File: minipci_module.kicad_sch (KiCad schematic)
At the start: 3 parts, among them Con2 2041119-1

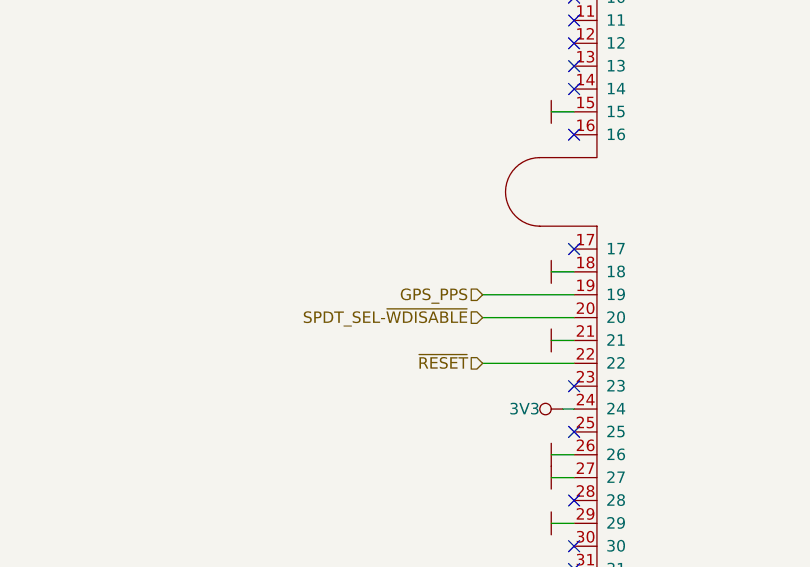
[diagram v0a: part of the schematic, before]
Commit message: Applied issue and regenerated gerbers
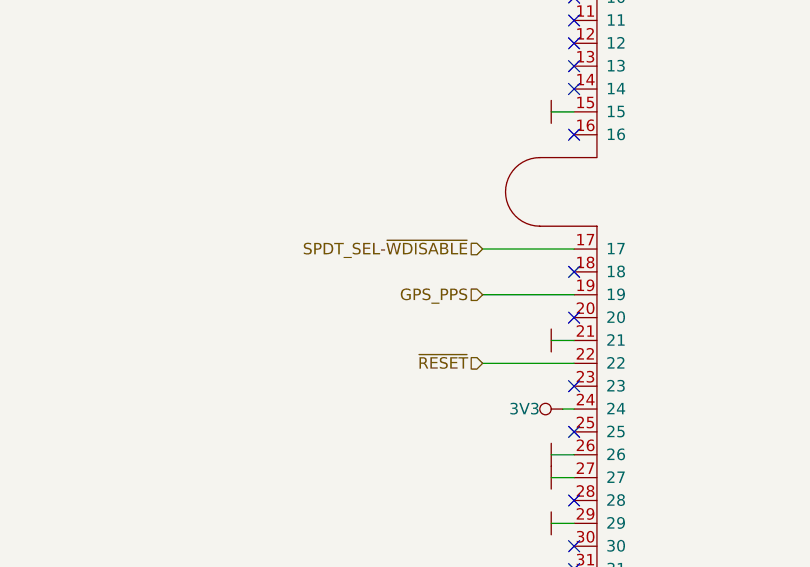
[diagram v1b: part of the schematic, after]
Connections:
- net GND: no longer Con2.18
- net SPDT_SEL-~WDISABLE~: now also Con2.17; no longer Con2.20
- no-connect marks 24 -> 25
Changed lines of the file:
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@@
   (no_connect (at 189.23 101.6))
   (no_connect (at 189.23 106.68))
-  (no_connect (at 189.23 119.38))
+  (no_connect (at 189.23 121.92))
+  (no_connect (at 189.23 127))
   (no_connect (at 189.23 134.62))
   (no_connect (at 189.23 139.7))
@@
     (stroke (width 0) (type solid) (color 0 0 0 0))
   )
+  (wire (pts (xy 179.07 119.38) (xy 189.23 119.38))
+    (stroke (width 0) (type solid) (color 0 0 0 0))
+  )
   (wire (pts (xy 179.07 205.74) (xy 189.23 205.74))
     (stroke (width 0) (type solid) (color 0 0 0 0))
@@
     (stroke (width 0) (type solid) (color 0 0 0 0))
   )
-  (wire (pts (xy 189.23 121.92) (xy 186.69 121.92))
-    (stroke (width 0) (type solid) (color 0 0 0 0))
-  )
   (wire (pts (xy 189.23 124.46) (xy 179.07 124.46))
     (stroke (width 0) (type solid) (color 0 0 0 0))
   )
-  (wire (pts (xy 189.23 127) (xy 179.07 127))
-    (stroke (width 0) (type solid) (color 0 0 0 0))
-  )
   (wire (pts (xy 189.23 129.54) (xy 186.69 129.54))
     (stroke (width 0) (type solid) (color 0 0 0 0))
@@
     (effects (font (size 1.27 1.27)) (justify right))
   )
+  (hierarchical_label "SPDT_SEL-~WDISABLE~" (shape input) (at 179.07 119.38 180)
+    (effects (font (size 1.27 1.27)) (justify right))
+  )
   (hierarchical_label "GPS_PPS" (shape input) (at 179.07 124.46 180)
     (effects (font (size 1.27 1.27)) (justify right))
   )
-  (hierarchical_label "SPDT_SEL-~WDISABLE~" (shape input) (at 179.07 127 180)
-    (effects (font (size 1.27 1.27)) (justify right))
-  )
   (hierarchical_label "~RESET~" (shape input) (at 179.07 132.08 180)
     (effects (font (size 1.27 1.27)) (justify right))
@@
       (effects (font (size 1.524 1.524)))
     )
-    (pin "1")
-  )
-  (symbol (lib_id "power:GND") (at 186.69 121.92 270) (unit 1)
-    (in_bom yes) (on_board yes)
-    (property "Reference" "#PWR011" (id 0) (at 189.23 121.92 0)
-      (effects (font (size 0.762 0.762)) hide)
-    )
-    (property "Value" "GND" (id 1) (at 184.15 121.92 0)
-      (effects (font (size 0.762 0.762)) hide)
-    )
-    (property "Footprint" "" (id 2) (at 186.69 121.92 0)
-      (effects (font (size 1.524 1.524)))
-    )
-    (property "Datasheet" "" (id 3) (at 186.69 121.92 0)
-      (effects (font (size 1.524 1.524)))
-    )
